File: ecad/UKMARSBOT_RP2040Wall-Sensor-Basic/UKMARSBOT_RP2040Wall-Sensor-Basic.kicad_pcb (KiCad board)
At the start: 2 copper layers, 80 x 31.2 mm, 32 parts, among them J1 Conn_01x16, Q1 BC337-40, Q2 BC337-40

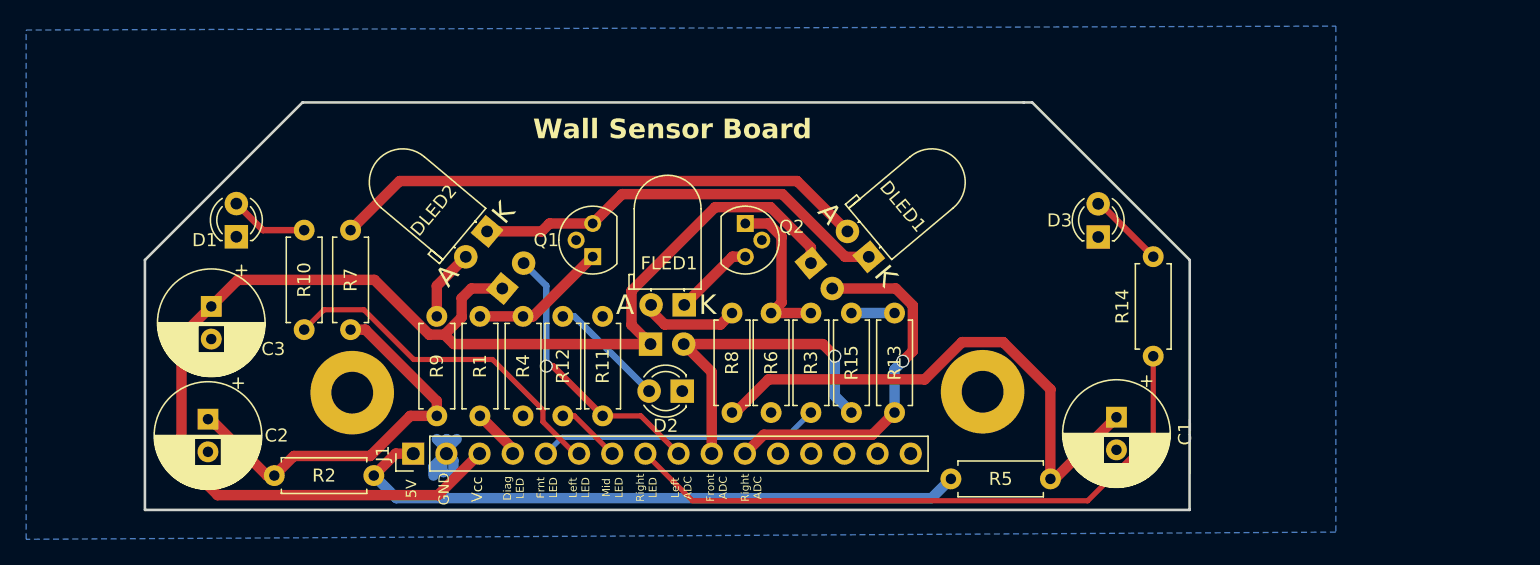
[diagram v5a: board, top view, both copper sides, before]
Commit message: Revised Wall Sensor Board consistent with hole and connector position. Fabrication files created.
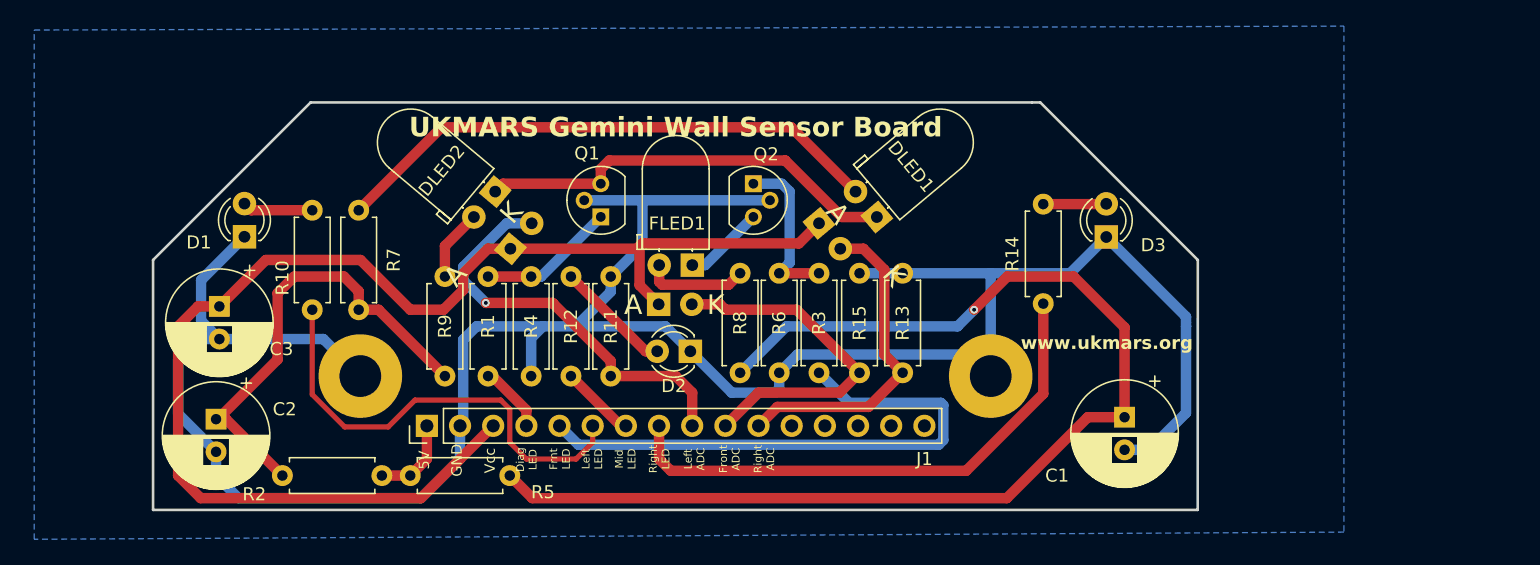
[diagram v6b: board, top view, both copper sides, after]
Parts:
- moved R5 41.4 mm to (120.3, 151.3)
- moved R14 9.33 mm to (168.8, 138.1)
- moved D2 3.11 mm to (141.8, 141.8)
- moved DLED1 3.11 mm to (156.1, 131.5)
- moved DLED2 3.11 mm to (126.8, 129.5)
- moved FPD1 3.11 mm to (139.3, 138.2)
- moved LDPD1 3.11 mm to (128.0, 133.9)
- moved Q1 3.11 mm to (134.9, 131.5)
- moved Q2 3.11 mm to (146.6, 128.9)
- moved R1 3.11 mm to (126.3, 143.7)
- moved R11 3.11 mm to (135.7, 143.7)
- moved R12 3.11 mm to (132.6, 143.7)
- moved R13 3.11 mm to (158.0, 143.4)
- moved R15 3.11 mm to (154.7, 143.4)
- moved R3 3.11 mm to (151.6, 143.4)
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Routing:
- net GND: track 12.2 -> 191.0 mm
- net Net-(C1-Pad1): track 42.0 -> 91.3 mm, vias 0 -> 1
- net 5V: track 49.2 -> 6.51 mm
- net SEN1DI0: track 21.6 -> 43.4 mm
- net SEN0AIP: track 21.5 -> 32.0 mm
- net SEN2DI0: track 26.8 -> 35.0 mm
- net SEN4DI0: track 48.5 -> 41.7 mm
- net Vcc: track 105.0 -> 100.2 mm
- net Net-(C2-Pad1): track 31.2 -> 35.9 mm
- net SEN2AIP: track 28.3 -> 25.2 mm, vias 1 -> 0
- net Net-(DLED1-A): track 41.2 -> 42.7 mm
- net SEN0DI0: track 3.93 -> 5.22 mm
- net SEN1AIP: track 26.1 -> 27.0 mm, vias 1 -> 0
- net Net-(D3-A): track 5.89 -> 5.01 mm
- net SEN3DI0: track 4.98 -> 5.78 mm
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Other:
- board text added: "UKMARS Gemini Wall Sensor Board"
- board text added: "www.ukmars.org"
- board text removed: "Wall Sensor Board"

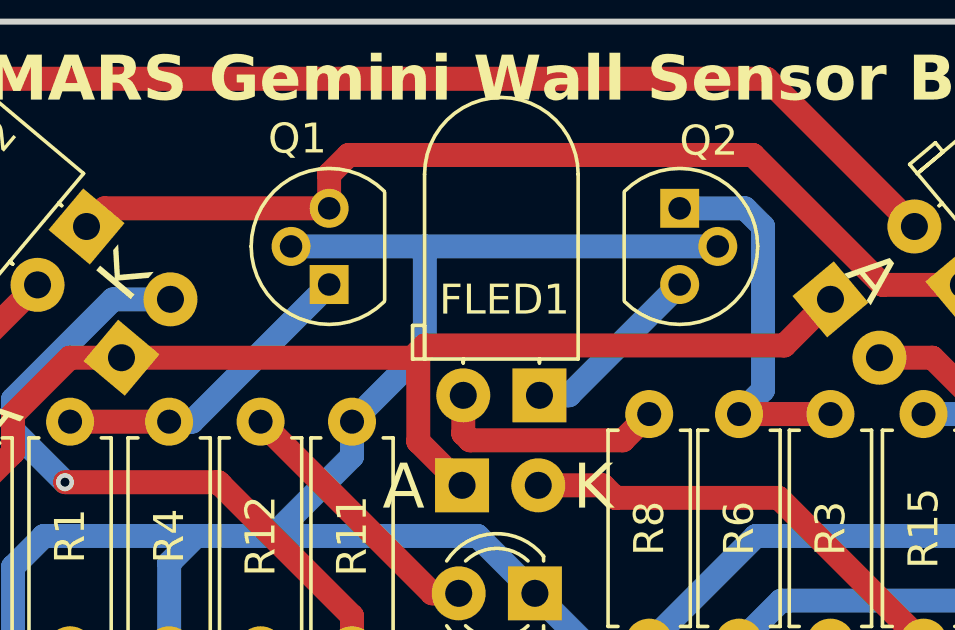
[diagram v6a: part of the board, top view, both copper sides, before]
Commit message: Fixed an issue with the transistor schematic being wrong for the wall sensor board.
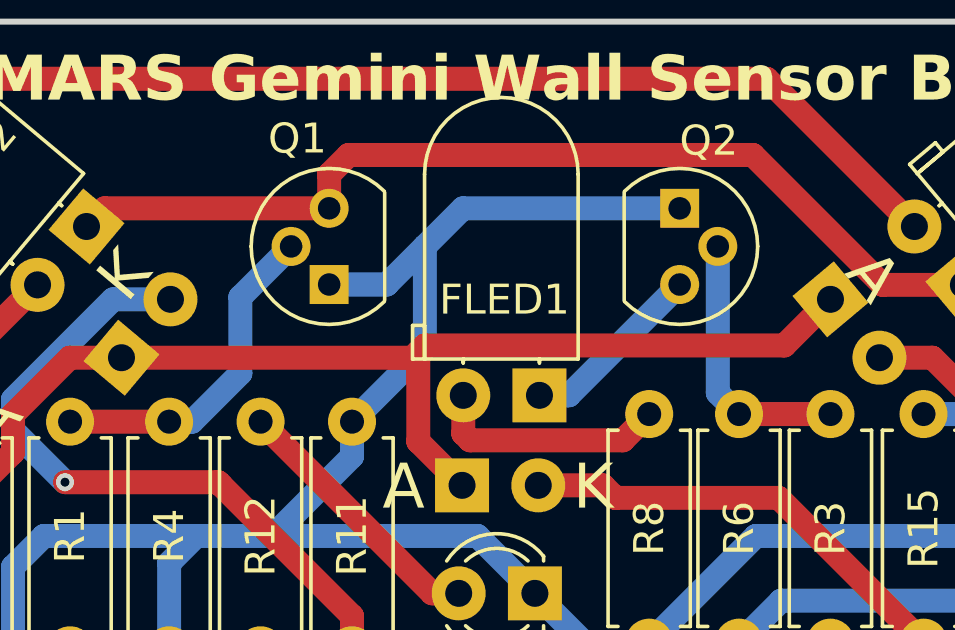
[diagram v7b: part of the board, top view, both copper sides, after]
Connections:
- Q1 pad 1: Net-(Q1-B) -> GND
- Q1 pad 2: GND -> Net-(Q1-B)
- Q2 pad 1: Net-(Q2-B) -> GND
- Q2 pad 2: GND -> Net-(Q2-E)
- R3 pad 2: Net-(Q2-B) -> Net-(Q2-E)
- R6 pad 1: Net-(Q2-B) -> Net-(Q2-E)
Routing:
- net Net-(Q2-B): track 12.7 -> 0.00 mm
- net Net-(Q2-E): track 0.00 -> 8.93 mm
- net GND: track 191.0 -> 189.6 mm
- net Net-(Q1-B): track 10.5 -> 11.3 mm

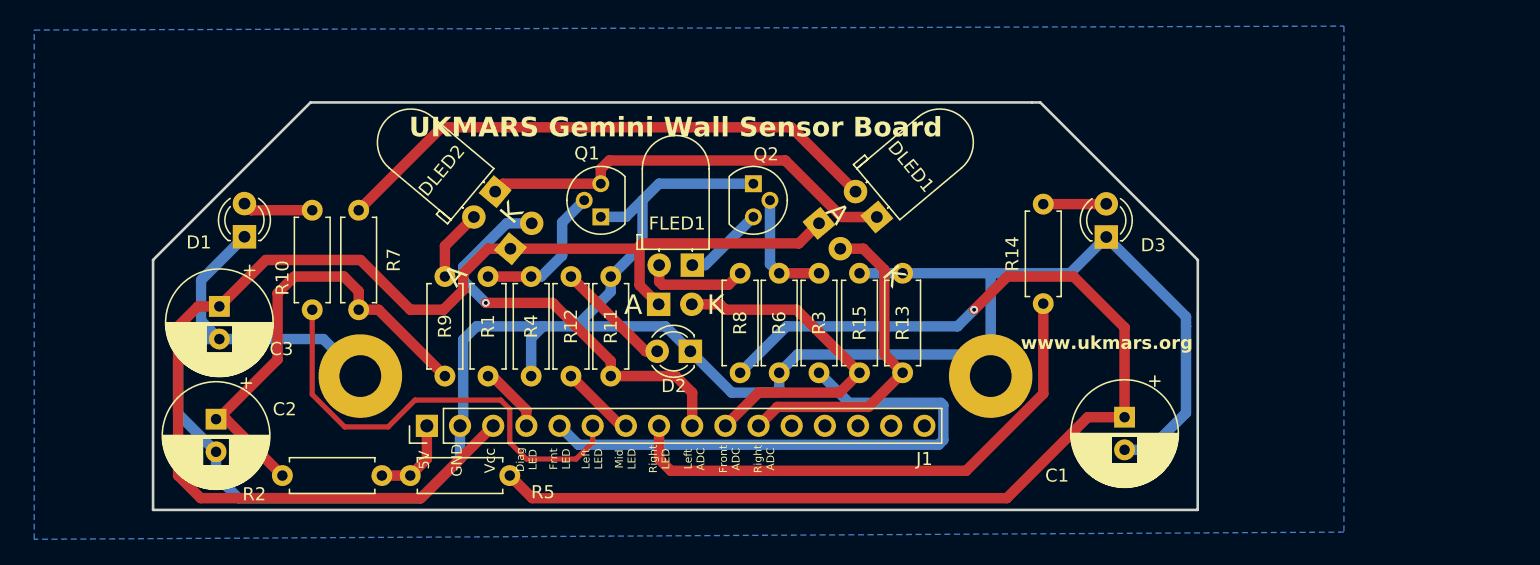
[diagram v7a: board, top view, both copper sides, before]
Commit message: Add v2 wall sensor board
Wall sensor updated for Issues raised on prototype builds. Better pin markings added to Line sensor, mezz and chassis boards
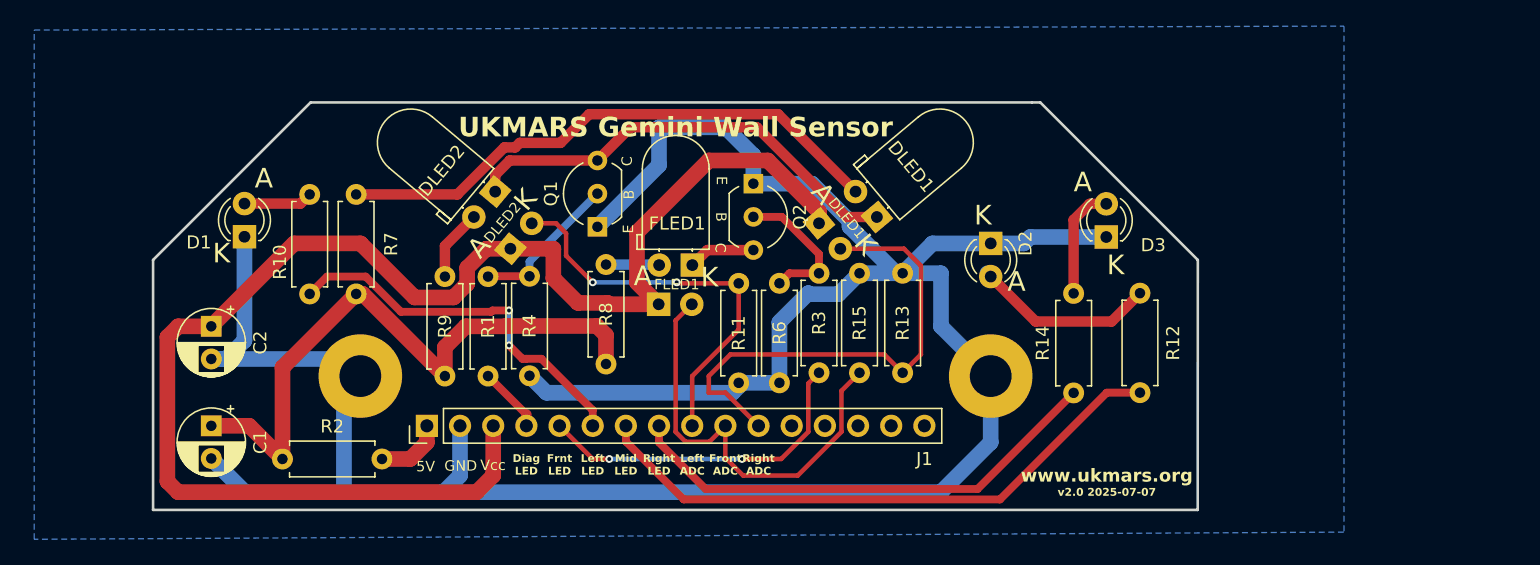
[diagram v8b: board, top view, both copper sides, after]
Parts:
- removed C3: 330uF, 16v, Capacitor_THT:CP_Radial_D8.0mm_P2.50mm
- removed R5: 33R, Resistor_THT:R_Axial_DIN0207_L6.3mm_D2.5mm_P7.62mm_Horizontal
- C1, C2: footprint Capacitor_THT:CP_Radial_D8.0mm_P2.50mm -> Capacitor_THT:CP_Radial_D5.0mm_P2.50mm
- FPD1, LDPD1, RDPD1: value BPW96B -> BPW85C; footprint LED_THT:LED_D5.0mm_Horizontal_O1.27mm_Z3.0mm -> LED_THT:LED_D3.0mm_Horizontal_O3.81mm_Z2.0mm
- Q1, Q2: footprint Package_TO_SOT_THT:TO-92 -> Package_TO_SOT_THT:TO-92_Inline_Wide
- R10, R12, R14: value 1K0 -> 680R
- R15: value 2k2 -> 1k8
- R7, R8, R9: value 33R -> 10R
- moved C1 69.9 mm to (105.1, 147.5)
- moved R12 43.6 mm to (176.2, 144.9)
- moved D2 24.4 mm to (164.8, 133.5), turned to -90 degrees
- moved R11 12.1 mm to (145.5, 136.5), turned to -90 degrees
- moved R8 10.3 mm to (135.3, 135.1)
- moved R14 7.22 mm to (171.1, 144.9)
- moved C2 7.12 mm to (105.1, 139.8)
- moved R2 1.27 mm to (118.2, 150.0)
- moved R10 1.23 mm to (112.6, 137.4)
- moved R7 1.23 mm to (116.2, 137.4)
- moved Q1 0.81 mm to (134.7, 132.2)
- moved R6 0.77 mm to (148.6, 136.5)
- moved R4 0.13 mm to (129.4, 136.0)
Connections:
- C1 pad 1: Net-(C1-Pad1) -> Vemit
- C2 pad 1: Net-(C2-Pad1) -> Vcc
- R2 pad 2: Net-(C2-Pad1) -> Vemit
- R7 pad 1: Net-(C2-Pad1) -> Vemit
- R8 pad 2: Net-(C1-Pad1) -> Vemit
- R9 pad 1: Net-(C2-Pad1) -> Vemit
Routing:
- net Net-(C1-Pad1): track 91.3 -> 0.00 mm, vias 1 -> 0
- net Vemit: track 0.00 -> 49.0 mm
- net SEN3DI0: track 5.78 -> 45.8 mm
- net Net-(C2-Pad1): track 35.9 -> 0.00 mm
- net SEN1DI0: track 43.4 -> 25.8 mm, vias 0 -> 2
- net GND: track 189.6 -> 205.1 mm
- net Vcc: track 100.2 -> 113.3 mm
- net SEN2AIP: track 25.2 -> 37.7 mm
- net SEN1AIP: track 27.0 -> 33.3 mm
- net SEN2DI0: track 35.0 -> 29.3 mm, vias 0 -> 2
- net Net-(D2-A): track 8.97 -> 14.1 mm
- net SEN4DI0: track 41.7 -> 37.5 mm
- net Net-(FLED1-A): track 7.93 -> 4.09 mm
- net Net-(D3-A): track 5.01 -> 8.64 mm
- net Net-(DLED1-K): track 32.7 -> 34.9 mm
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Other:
- board text added: "B"
- board text added: "DLED1"
- board text added: "DLED2"
- board text added: "FLED1"
- board text added: "R4"
- board text added: "UKMARS Gemini Wall Sensor"
- board text added: "Version 2.0"
- board text added: "v2.0 2025-07-07"
- board text removed: "UKMARS Gemini Wall Sensor Board"
- board text removed: "Version ${version}"
